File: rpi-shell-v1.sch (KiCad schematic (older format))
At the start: 29 parts, among them Q1 Q_PMOS_SGD, Q2 Q_PMOS_SGD, SW1 L1, SW2 L2, SW3 Select, SW4 Start, SW5 R2, SW6 R1, U1 Thumbstick, U2 dpad-cross-trace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

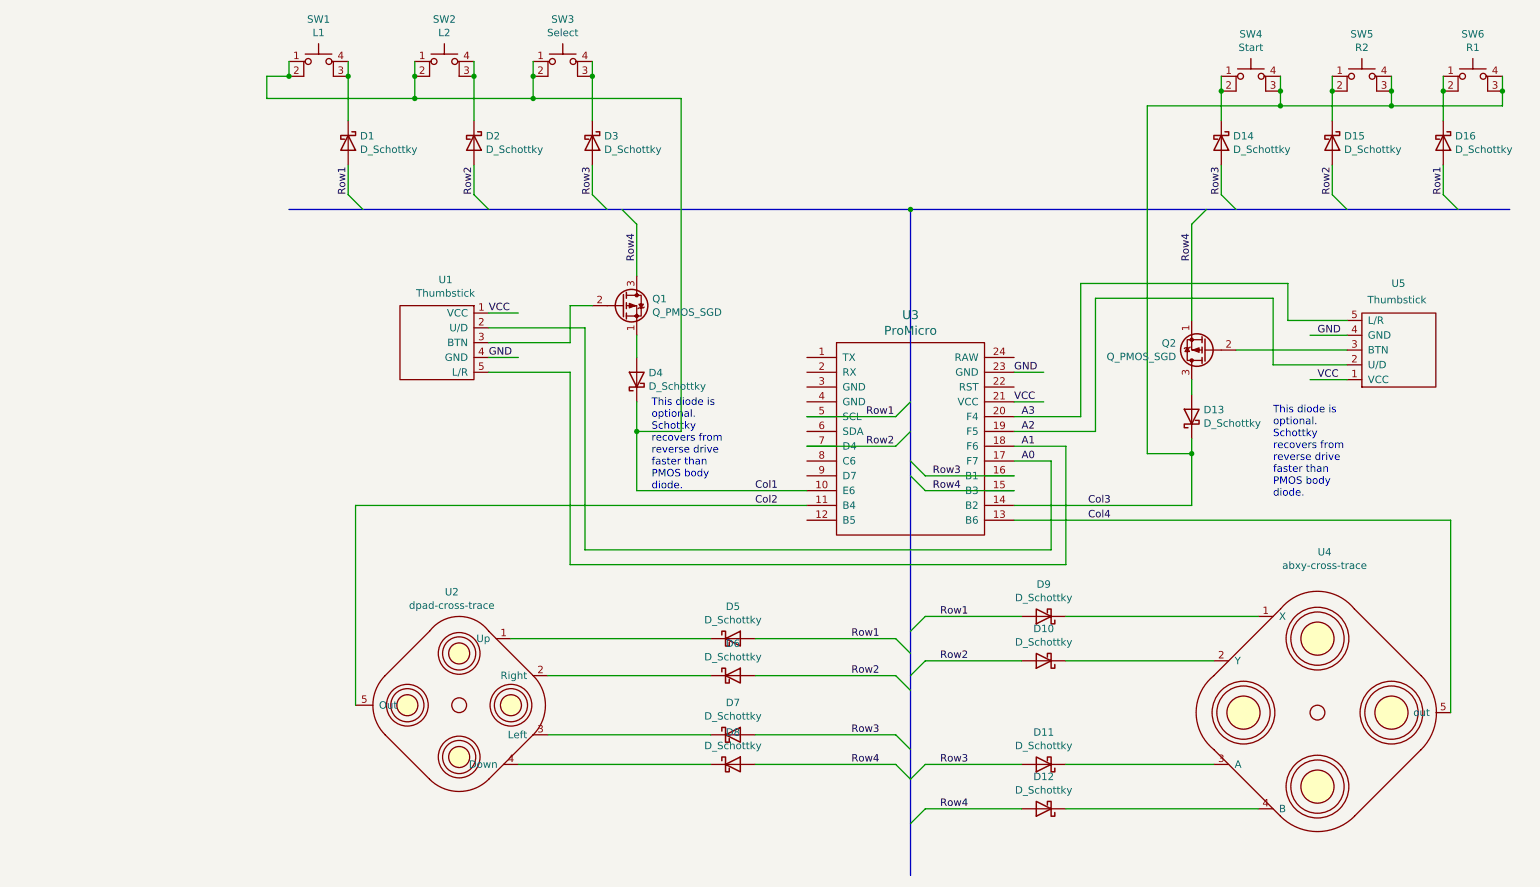
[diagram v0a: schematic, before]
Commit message: Convert schematics to hierarchy.
Move current schematics into a controller subsystem schematic page
and create an audio subsystem schematic page.
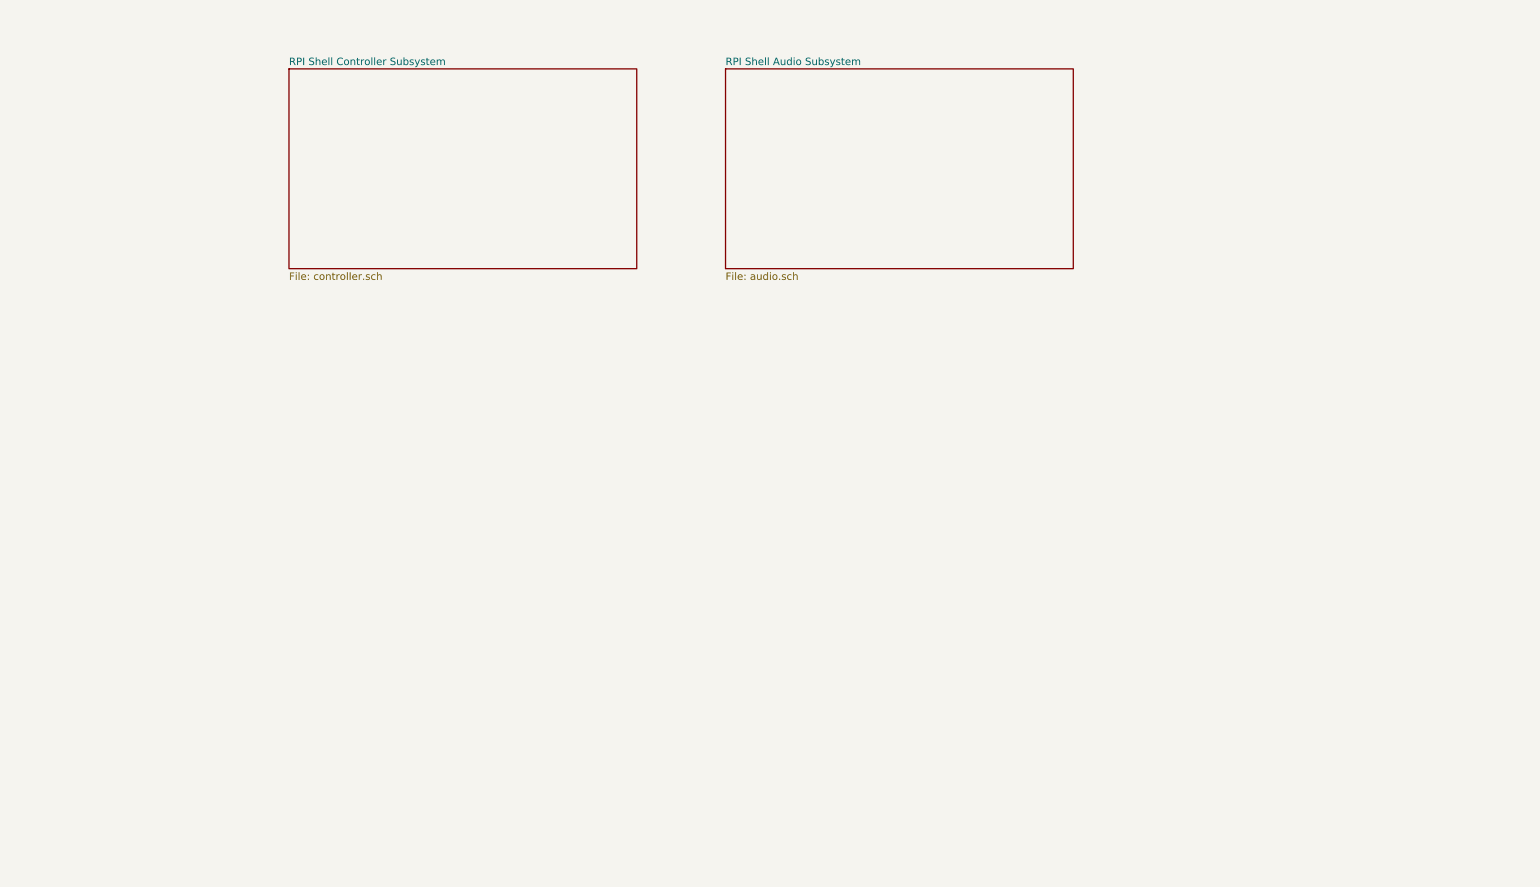
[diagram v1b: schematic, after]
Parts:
- removed D1, D10, D11, D12, D13, D14, D15, D16, D2, D3, D4, D5, D6, D7, D8, D9: D_Schottky, symbol Device:D_Schottky
- removed Q1, Q2: Q_PMOS_SGD, symbol Device:Q_PMOS_SGD
- removed SW1: L1, symbol Switch:SW_MEC_5E
- removed SW2: L2, symbol Switch:SW_MEC_5E
- removed SW3: Select, symbol Switch:SW_MEC_5E
- removed SW4: Start, symbol Switch:SW_MEC_5E
- removed SW5: R2, symbol Switch:SW_MEC_5E
- removed SW6: R1, symbol Switch:SW_MEC_5E
- removed U1, U5: Thumbstick, symbol rpi-shell:Thumbstick
- removed U2: dpad-cross-trace, symbol rpi-shell:dpad-cross-trace
- removed U3: ProMicro, symbol promicro:ProMicro
- removed U4: abxy-cross-trace, symbol rpi-shell:abxy-cross-trace
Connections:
- net labels removed: A0, A1, A2, A3, Col1, Col2, Col3, Col4, GND, Row1, Row2, Row3, Row4, VCC
- wire segments 105 -> 0
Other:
- note removed: "This diode is\noptional.\nSchottky\nrecovers from\nreverse drive\nfaster than \nPMOS body \ndiode.\n"

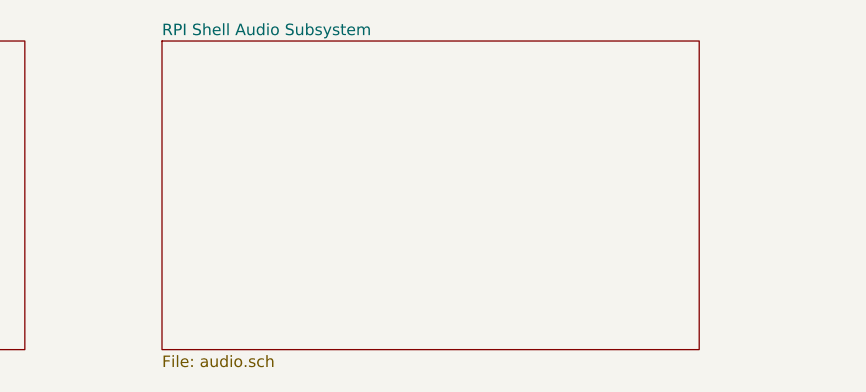
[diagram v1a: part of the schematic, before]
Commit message: Add LM386 amp circuits and hierarchy pins.
Add two LM386 amplifier circuit schematics to audio subsystem.
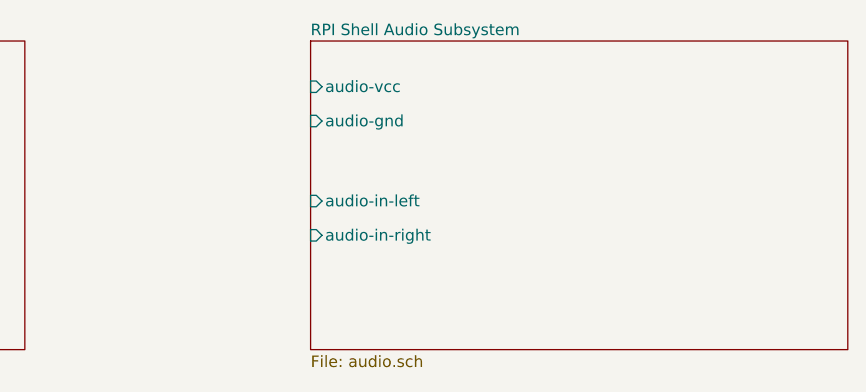
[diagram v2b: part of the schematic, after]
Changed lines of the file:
@@
 $EndSheet
 $Sheet
-S 4350 1200 2350 1350
+S 5000 1200 2350 1350
 U 6068502A
 F0 "RPI Shell Audio Subsystem" 50
 F1 "audio.sch" 50
+F2 "audio-vcc" I L 5000 1400 50
+F3 "audio-gnd" I L 5000 1550 50
+F4 "audio-in-left" I L 5000 1900 50
+F5 "audio-in-right" I L 5000 2050 50
 $EndSheet
 $EndSCHEMATC

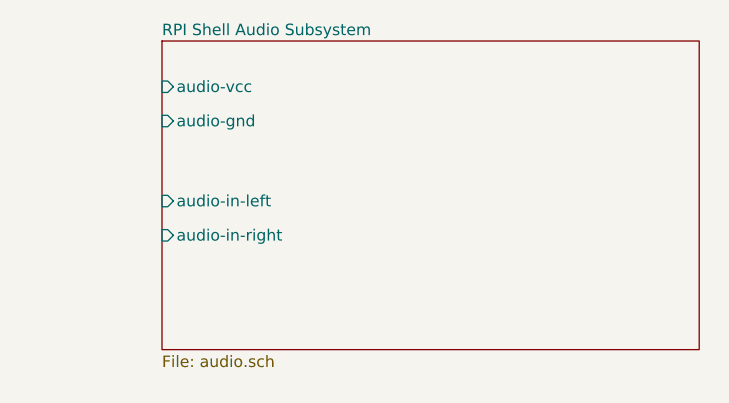
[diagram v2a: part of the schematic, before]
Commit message: Implement Adafruit I2S stereo decoder symbol.
Add stereo decoder to audio subsystem schematic. NOTE: the adafruit
library may be separated out later if necessary. Change hierarchical
schematic pins coming in/out of the audio subsystem.
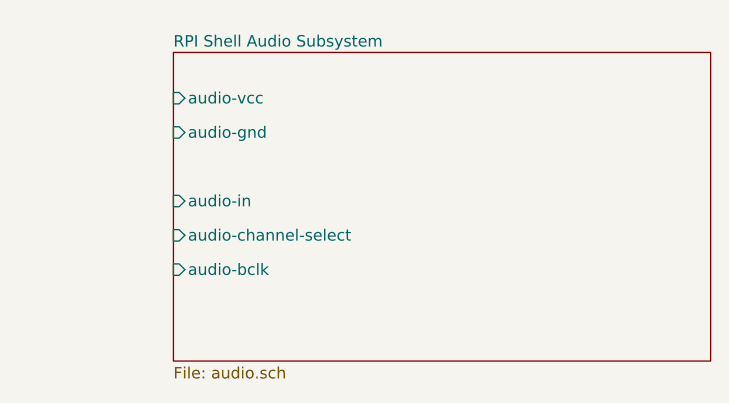
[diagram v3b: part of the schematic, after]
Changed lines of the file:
@@
 $EndSheet
 $Sheet
-S 5000 1200 2350 1350
+S 5050 1250 2350 1350
 U 6068502A
 F0 "RPI Shell Audio Subsystem" 50
 F1 "audio.sch" 50
-F2 "audio-vcc" I L 5000 1400 50
-F3 "audio-gnd" I L 5000 1550 50
-F4 "audio-in-left" I L 5000 1900 50
-F5 "audio-in-right" I L 5000 2050 50
+F2 "audio-vcc" I L 5050 1450 50
+F3 "audio-gnd" I L 5050 1600 50
+F4 "audio-in" I L 5050 1900 50
+F5 "audio-channel-select" I L 5050 2050 50
+F6 "audio-bclk" I L 5050 2200 50
 $EndSheet
 $EndSCHEMATC

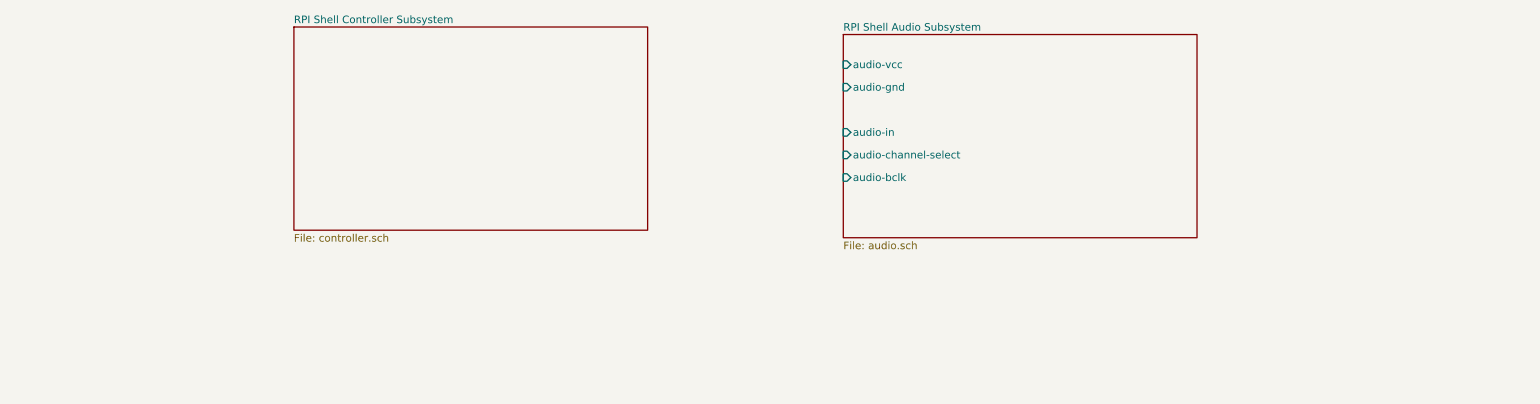
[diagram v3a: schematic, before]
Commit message: Fix power pins to remove ERC warnings.
Add global VCC and GND power pins. Add PWR_FLAG to Arduino VCC and to
audio subsystem power pins to remove ERC warnings.

Add Not Connected to all applicable pins.
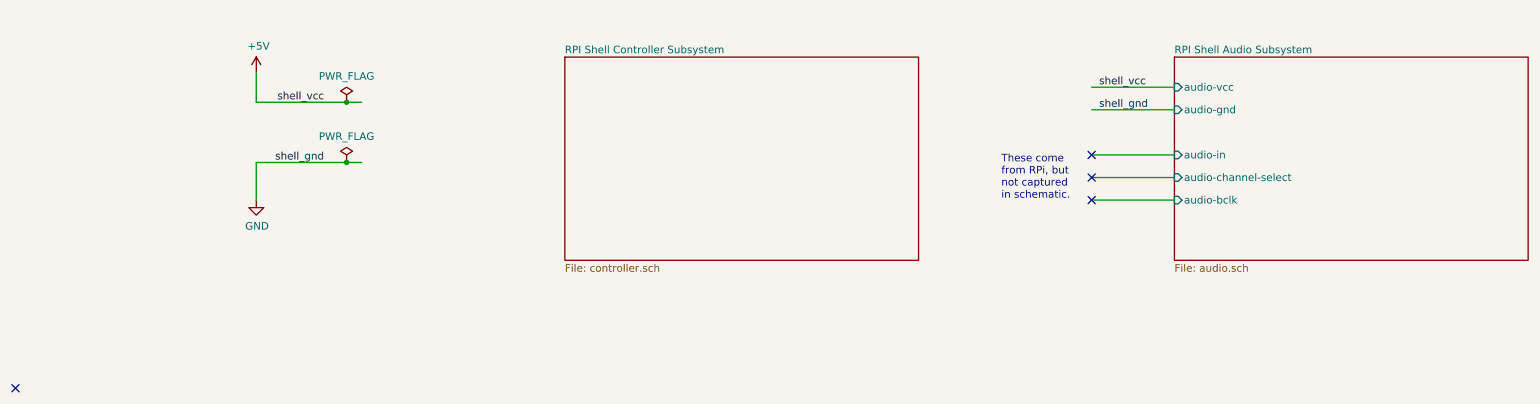
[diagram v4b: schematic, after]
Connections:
- net labels added: +5V, GND, shell_gnd, shell_vcc
- wire segments 0 -> 11
- no-connect marks 0 -> 4
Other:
- note added: "These come\nfrom RPi, but\nnot captured\nin schematic."
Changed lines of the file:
@@
 $EndDescr
 $Sheet
-S 1400 1200 2350 1350
+S 3200 1400 2350 1350
 U 6065582D
 F0 "RPI Shell Controller Subsystem" 50
@@
 $EndSheet
 $Sheet
-S 5050 1250 2350 1350
+S 7250 1400 2350 1350
 U 6068502A
 F0 "RPI Shell Audio Subsystem" 50
 F1 "audio.sch" 50
-F2 "audio-vcc" I L 5050 1450 50
-F3 "audio-gnd" I L 5050 1600 50
-F4 "audio-in" I L 5050 1900 50
-F5 "audio-channel-select" I L 5050 2050 50
-F6 "audio-bclk" I L 5050 2200 50
+F2 "audio-vcc" I L 7250 1600 50
+F3 "audio-gnd" I L 7250 1750 50
+F4 "audio-in" I L 7250 2050 50
+F5 "audio-channel-select" I L 7250 2200 50
+F6 "audio-bclk" I L 7250 2350 50
 $EndSheet
+Wire Wire Line
+	1150 1500 1150 1700
+Wire Wire Line
+	1150 2350 1150 2100
+Text Label 1600 1700 2    50   ~ 0
+shell_vcc
+Text Label 1600 2100 2    50   ~ 0
+shell_gnd
+Wire Wire Line
+	7250 1600 6700 1600
+Wire Wire Line
+	7250 1750 6700 1750
+Text Label 6750 1600 0    50   ~ 0
+shell_vcc
+Text Label 6750 1750 0    50   ~ 0
+shell_gnd
+Wire Wire Line
+	7250 2050 6700 2050
+NoConn ~ 6700 2050
+Wire Wire Line
+	7250 2200 6700 2200
+Wire Wire Line
+	7250 2350 6700 2350
+NoConn ~ 6700 2200
+NoConn ~ 6700 2350
+NoConn ~ -450 3600
+$Comp
+L power:+5V #PWR0101
+U 1 1 606A65CF
+P 1150 1500
+F 0 "#PWR0101" H 1150 1350 50  0001 C CNN
+F 1 "+5V" H 1165 1673 50  0000 C CNN
+F 2 "" H 1150 1500 50  0001 C CNN
+F 3 "" H 1150 1500 50  0001 C CNN
+	1    1150 1500
+	1    0    0    -1
+$EndComp
+$Comp
+L power:GND #PWR0102
+U 1 1 606A6EC7
+P 1150 2350
+F 0 "#PWR0102" H 1150 2100 50  0001 C CNN
+F 1 "GND" H 1155 2177 50  0000 C CNN
+F 2 "" H 1150 2350 50  0001 C CNN
+F 3 "" H 1150 2350 50  0001 C CNN
+	1    1150 2350
+	1    0    0    -1
+$EndComp
+Wire Wire Line
+	1150 1700 1750 1700
+Wire Wire Line
+	1150 2100 1750 2100
+$Comp
+L power:PWR_FLAG #FLG0101
+U 1 1 606AE24D
+P 1750 1700
+F 0 "#FLG0101" H 1750 1775 50  0001 C CNN
+F 1 "PWR_FLAG" H 1750 1873 50  0000 C CNN
+F 2 "" H 1750 1700 50  0001 C CNN
+F 3 "~" H 1750 1700 50  0001 C CNN
+	1    1750 1700
+	1    0    0    -1
+$EndComp
+Connection ~ 1750 1700
+Wire Wire Line
+	1750 1700 1850 1700
+$Comp
+L power:PWR_FLAG #FLG0102
+U 1 1 606AE818
+P 1750 2100
+F 0 "#FLG0102" H 1750 2175 50  0001 C CNN
+F 1 "PWR_FLAG" H 1750 2273 50  0000 C CNN
+F 2 "" H 1750 2100 50  0001 C CNN
+F 3 "~" H 1750 2100 50  0001 C CNN
+	1    1750 2100
+	1    0    0    -1
+$EndComp
+Connection ~ 1750 2100
+Wire Wire Line
+	1750 2100 1850 2100
+Text Notes 6100 2350 0    50   ~ 0
+These come\nfrom RPi, but\nnot captured\nin schematic.
 $EndSCHEMATC

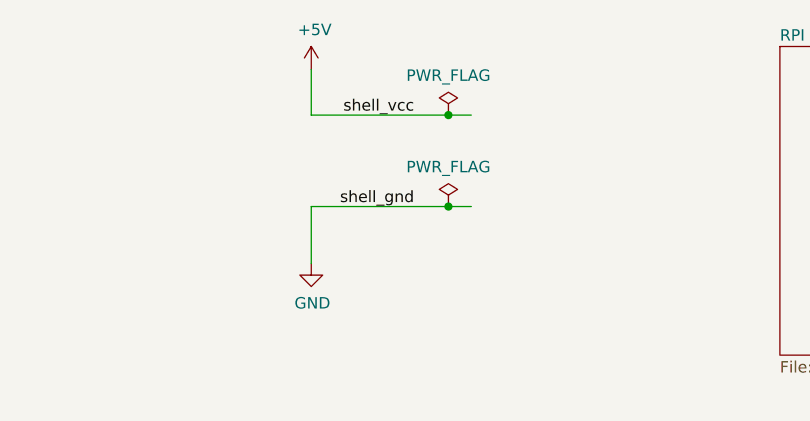
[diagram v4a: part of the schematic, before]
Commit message: Move most PWR_FLAGs into corner and use GNDA.
Use GNDA power pin in the audio subsystem instead of "agnd" sheet label.
Re-examine application of PWR_FLAGS after reading the wiki page.

Change the symbol for thumbstick in controller subsystem to reflect that
it's actually the FPC connector and not actually the thumbstick module.
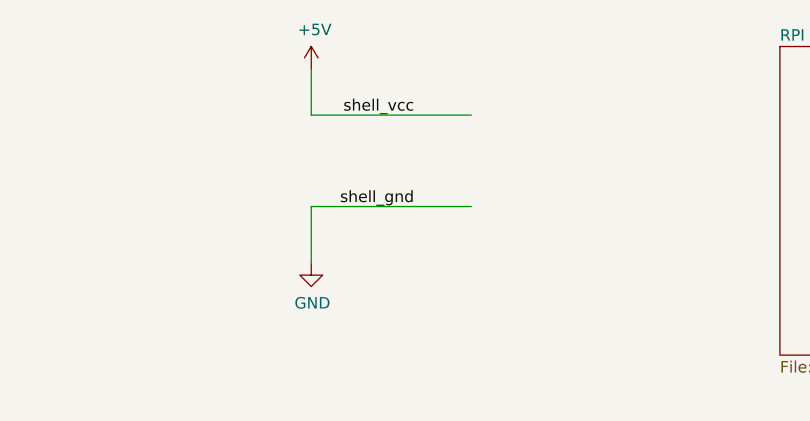
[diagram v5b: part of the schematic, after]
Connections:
- wire segments 11 -> 9
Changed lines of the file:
@@
 Comment4 ""
 $EndDescr
-$Sheet
-S 3200 1400 2350 1350
-U 6065582D
-F0 "RPI Shell Controller Subsystem" 50
-F1 "controller.sch" 50
-$EndSheet
-$Sheet
-S 7250 1400 2350 1350
-U 6068502A
-F0 "RPI Shell Audio Subsystem" 50
-F1 "audio.sch" 50
-F2 "audio-vcc" I L 7250 1600 50
-F3 "audio-gnd" I L 7250 1750 50
-F4 "audio-in" I L 7250 2050 50
-F5 "audio-channel-select" I L 7250 2200 50
-F6 "audio-bclk" I L 7250 2350 50
-$EndSheet
 Wire Wire Line
 	1150 1500 1150 1700
@@
 Text Label 1600 2100 2    50   ~ 0
 shell_gnd
-Wire Wire Line
-	7250 1600 6700 1600
-Wire Wire Line
-	7250 1750 6700 1750
-Text Label 6750 1600 0    50   ~ 0
-shell_vcc
-Text Label 6750 1750 0    50   ~ 0
-shell_gnd
-Wire Wire Line
-	7250 2050 6700 2050
-NoConn ~ 6700 2050
-Wire Wire Line
-	7250 2200 6700 2200
-Wire Wire Line
-	7250 2350 6700 2350
-NoConn ~ 6700 2200
-NoConn ~ 6700 2350
 NoConn ~ -450 3600
 $Comp
@@
 $EndComp
 Wire Wire Line
-	1150 1700 1750 1700
+	1150 2100 1850 2100
 Wire Wire Line
-	1150 2100 1750 2100
-$Comp
-L power:PWR_FLAG #FLG0101
-U 1 1 606AE24D
-P 1750 1700
-F 0 "#FLG0101" H 1750 1775 50  0001 C CNN
-F 1 "PWR_FLAG" H 1750 1873 50  0000 C CNN
-F 2 "" H 1750 1700 50  0001 C CNN
-F 3 "~" H 1750 1700 50  0001 C CNN
-	1    1750 1700
-	1    0    0    -1
-$EndComp
-Connection ~ 1750 1700
-Wire Wire Line
-	1750 1700 1850 1700
-$Comp
-L power:PWR_FLAG #FLG0102
-U 1 1 606AE818
-P 1750 2100
-F 0 "#FLG0102" H 1750 2175 50  0001 C CNN
-F 1 "PWR_FLAG" H 1750 2273 50  0000 C CNN
-F 2 "" H 1750 2100 50  0001 C CNN
-F 3 "~" H 1750 2100 50  0001 C CNN
-	1    1750 2100
-	1    0    0    -1
-$EndComp
-Connection ~ 1750 2100
-Wire Wire Line
-	1750 2100 1850 2100
+	1150 1700 1850 1700
 Text Notes 6100 2350 0    50   ~ 0
 These come\nfrom RPi, but\nnot captured\nin schematic.
+NoConn ~ 6700 2350
+NoConn ~ 6700 2200
+Wire Wire Line
+	7250 2350 6700 2350
+Wire Wire Line
+	7250 2200 6700 2200
+NoConn ~ 6700 2050
+Wire Wire Line
+	7250 2050 6700 2050
+Text Label 6750 1750 0    50   ~ 0
+shell_gnd
+Text Label 6750 1600 0    50   ~ 0
+shell_vcc
+Wire Wire Line
+	7250 1750 6700 1750
+Wire Wire Line
+	7250 1600 6700 1600
+$Sheet
+S 7250 1400 2350 1350
+U 6068502A
+F0 "RPI Shell Audio Subsystem" 50
+F1 "audio.sch" 50
+F2 "audio-vcc" I L 7250 1600 50
+F3 "audio-gnd" I L 7250 1750 50
+F4 "audio-in" I L 7250 2050 50
+F5 "audio-channel-select" I L 7250 2200 50
+F6 "audio-bclk" I L 7250 2350 50
+$EndSheet
+$Sheet
+S 3200 1400 2350 1350
+U 6065582D
+F0 "RPI Shell Controller Subsystem" 50
+F1 "controller.sch" 50
+$EndSheet
 $EndSCHEMATC
